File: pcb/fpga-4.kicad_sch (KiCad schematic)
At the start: 1 part, among them U5 XC7A100T-FGG484

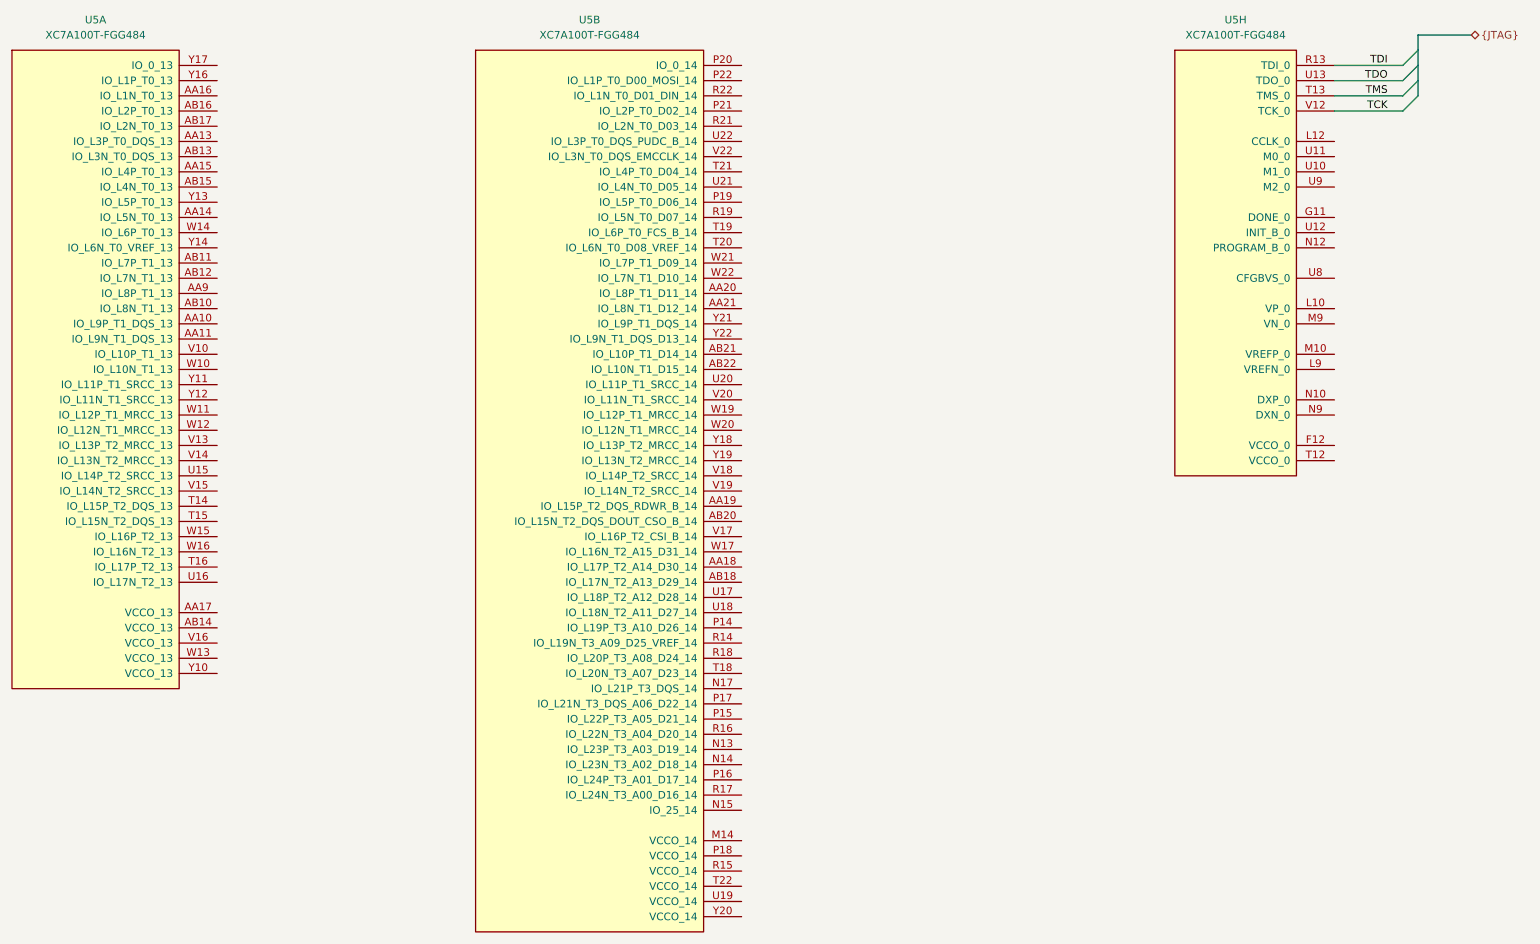
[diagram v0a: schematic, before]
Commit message: defined memory pinouts
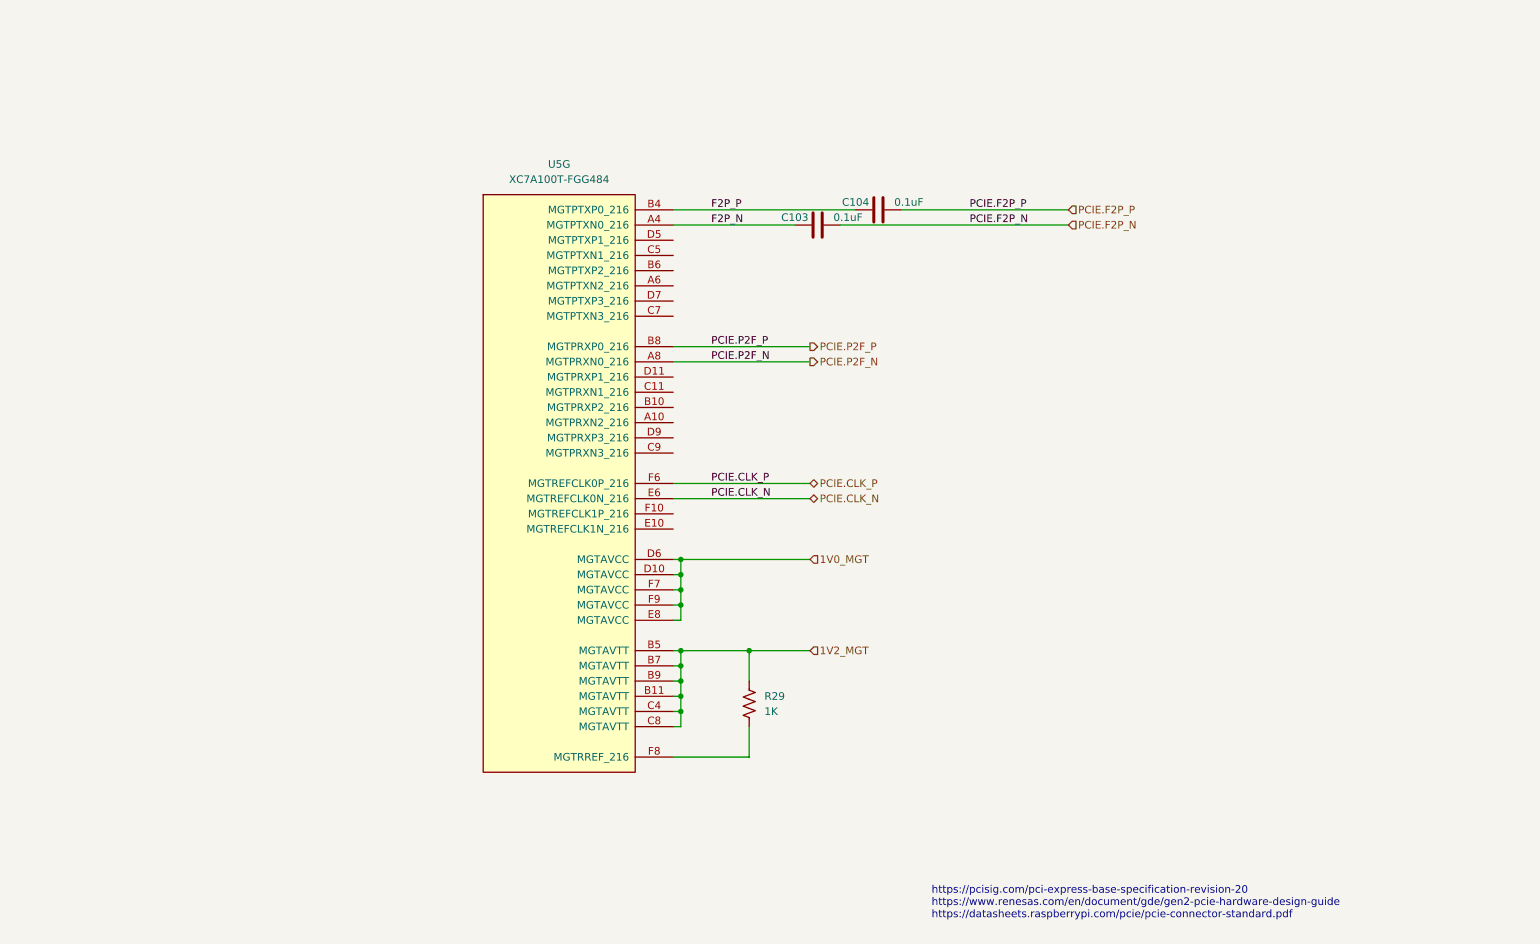
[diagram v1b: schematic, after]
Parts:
- removed U5: XC7A100T-FGG484, library:Xilinx_FGG484, symbol FPGA_Xilinx_Artix7:XC7A100T-FGG484
- added C103, C104: 0.1uF, Capacitor_SMD:C_0402_1005Metric, symbol library:C
- added R29: 1K, symbol library:R_US
- added U5: XC7A100T-FGG484, library:Xilinx_FGG484, symbol FPGA_Xilinx_Artix7:XC7A100T-FGG484
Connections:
- new net: R29.1, U5.F8 (MGTRREF_216)
- new net 1V0_MGT: U5.D10 (MGTAVCC), U5.D6 (MGTAVCC), U5.E8 (MGTAVCC), U5.F7 (MGTAVCC), U5.F9 (MGTAVCC)
- new net 1V2_MGT: R29.2, U5.B11 (MGTAVTT), U5.B5 (MGTAVTT), U5.B7 (MGTAVTT), U5.B9 (MGTAVTT), U5.C4 (MGTAVTT), U5.C8 (MGTAVTT)
- new net F2P_N: C103.1, U5.A4 (MGTPTXN0_216)
- new net F2P_P: C104.1, U5.B4 (MGTPTXP0_216)
- new net PCIE.CLK_N: U5.E6 (MGTREFCLK0N_216)
- new net PCIE.CLK_P: U5.F6 (MGTREFCLK0P_216)
- new net PCIE.F2P_N: C103.2
- new net PCIE.F2P_P: C104.2
- new net PCIE.P2F_N: U5.A8 (MGTPRXN0_216)
- new net PCIE.P2F_P: U5.B8 (MGTPRXP0_216)
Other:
- note added: "https://pcisig.com/pci-express-base-specification-revision-20 https://www.renesas.com/en/document/gde/gen2-pcie-hardware-design-guide https://datasheets.raspberrypi.com/pcie/pcie-connector-standard.pdf"

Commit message: power restructuring
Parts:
- removed C103, C104: 0.1uF, Capacitor_SMD:C_0402_1005Metric, symbol library:C
- added C11, C12: 0.1uF, Capacitor_SMD:C_0402_1005Metric, symbol library:C
- U5: symbol FPGA_Xilinx_Artix7:XC7A100T-FGG484 -> library:XC7A100T-FGG484
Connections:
- net F2P_N: now also C11.1
- net F2P_P: now also C12.1
- net PCIE.F2P_N: now also C11.2
- net PCIE.F2P_P: now also C12.2
- net at U5.F8 (MGTRREF_216): no longer R29.1
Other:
- moved on the sheet: R29, U5G

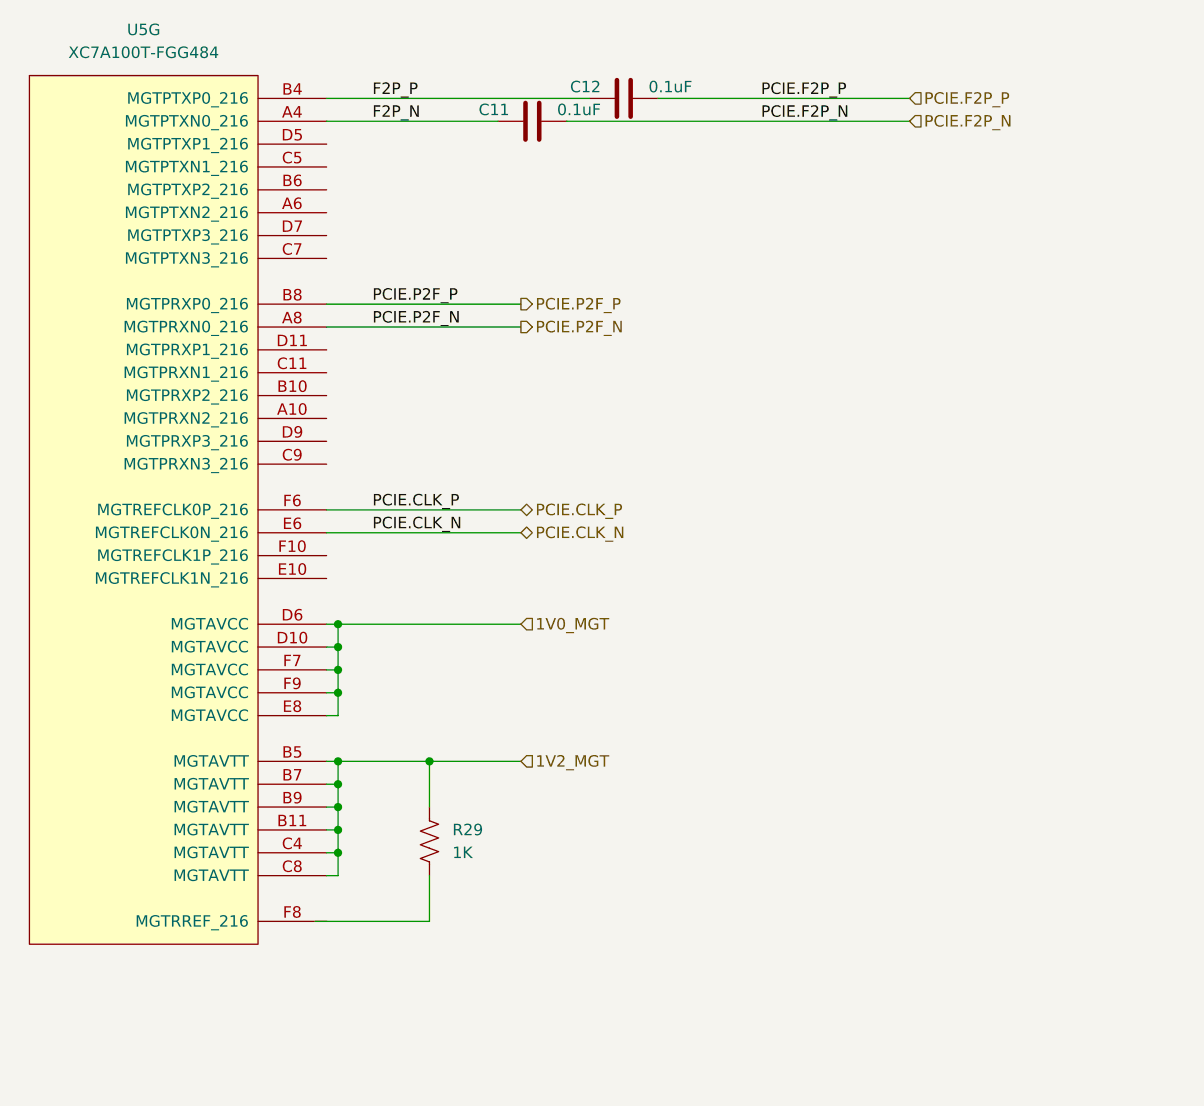
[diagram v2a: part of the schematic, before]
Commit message: changes to power tree
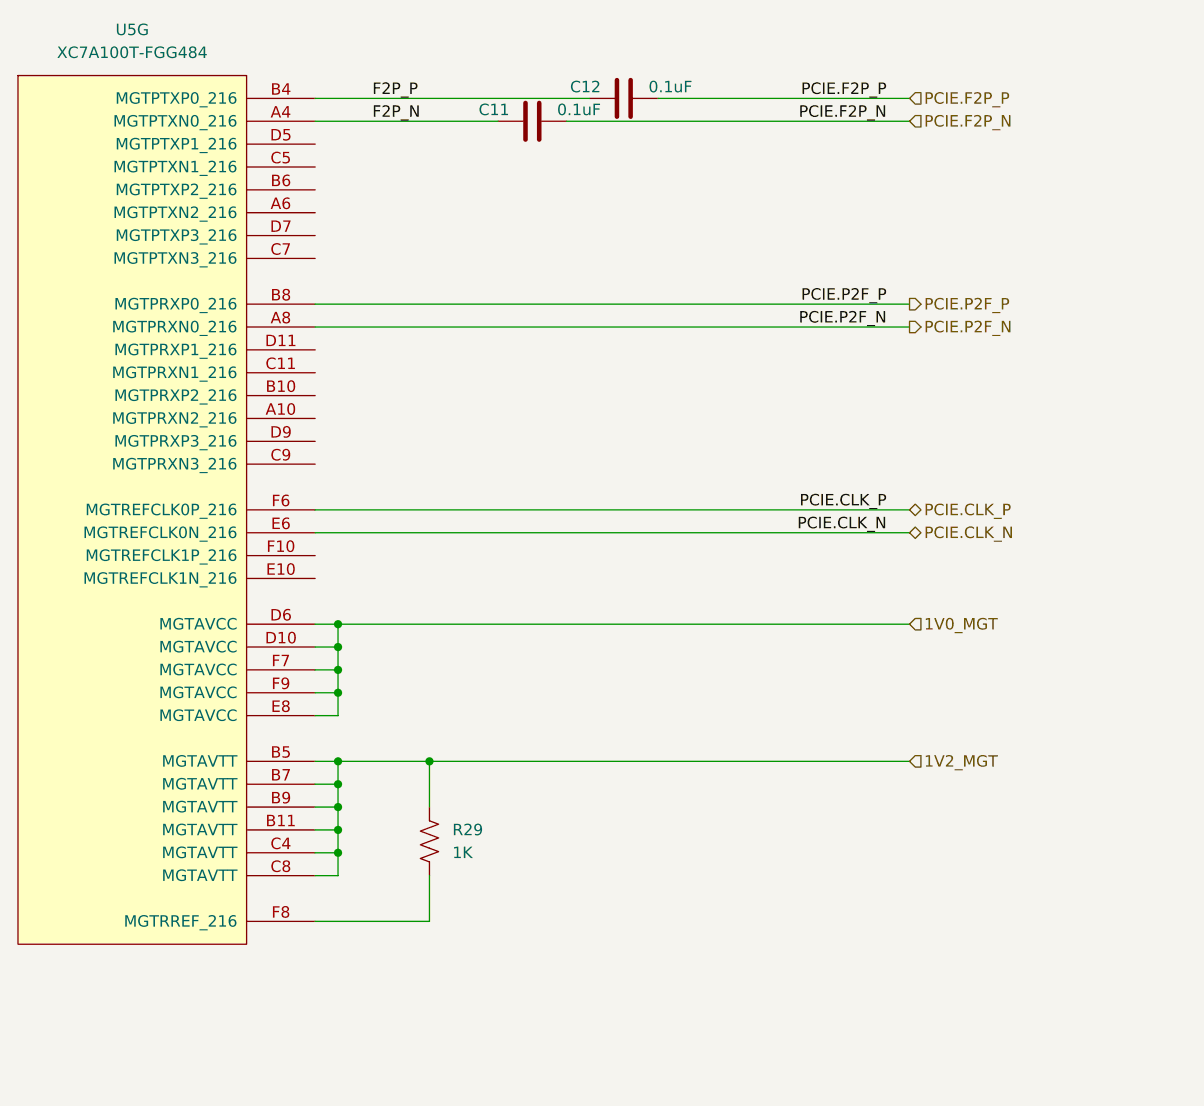
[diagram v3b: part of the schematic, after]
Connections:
- net at U5.F8 (MGTRREF_216): now also R29.1
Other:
- moved on the sheet: U5G

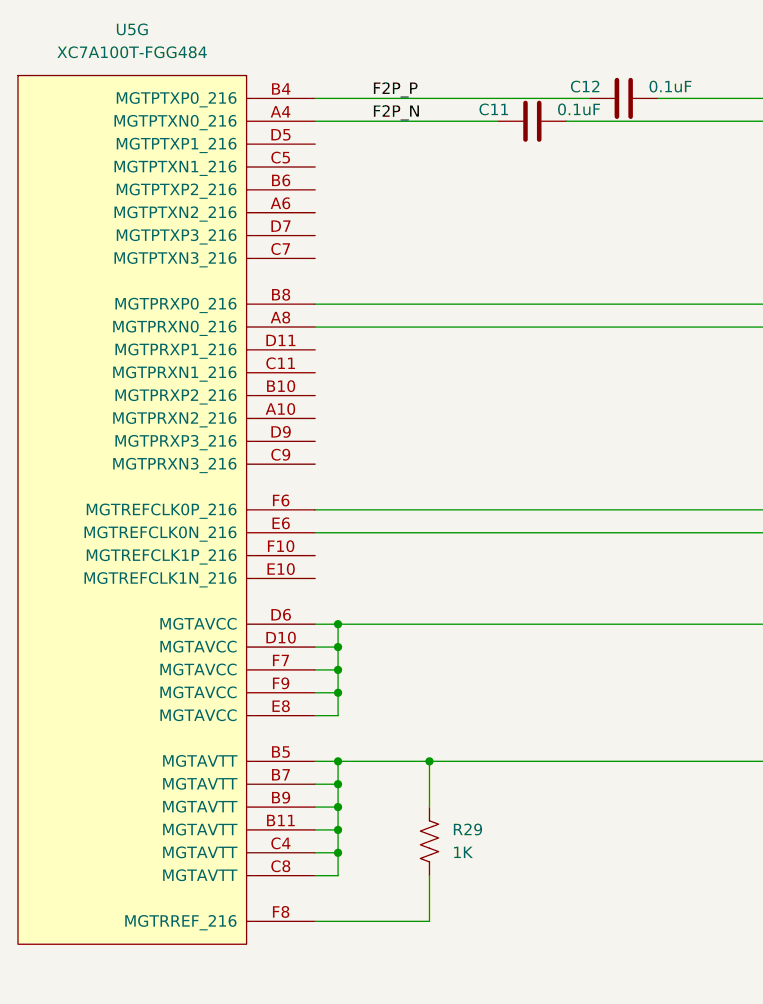
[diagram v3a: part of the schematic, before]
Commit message: moved stuff around, bom
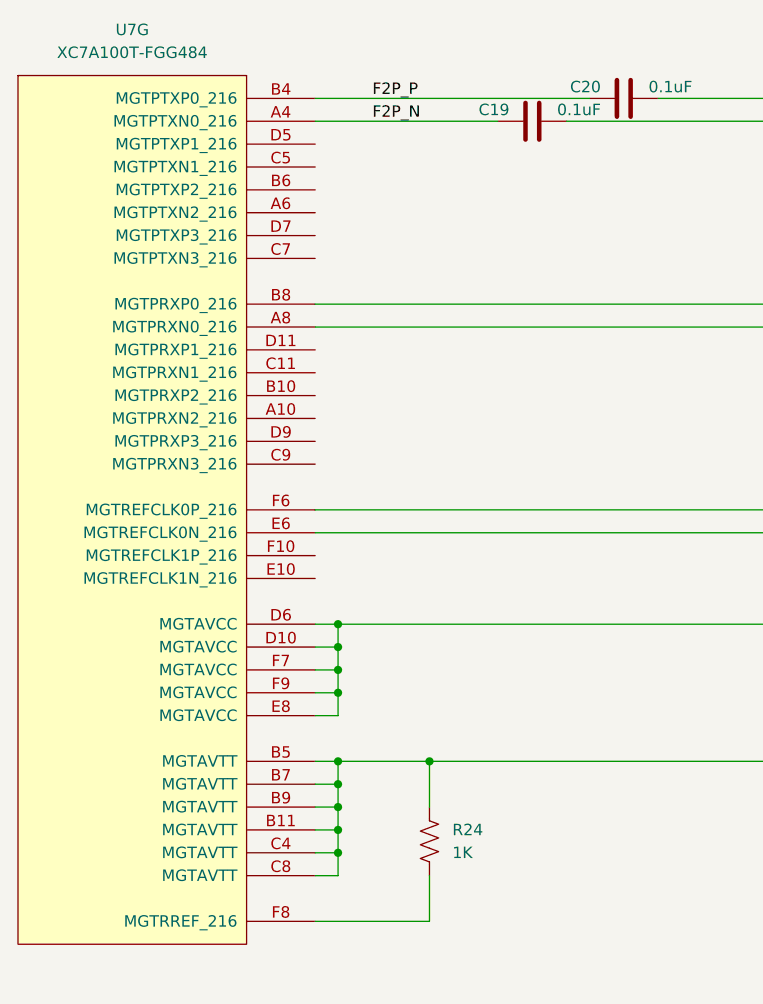
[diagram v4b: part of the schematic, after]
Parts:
- renumbered C11 to C19, C12 to C20, R29 to R24, U5 to U7
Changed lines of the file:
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@@
 		(dnp no)
 		(fields_autoplaced yes)
-		(property "Reference" "U5"
+		(property "Reference" "U7"
 			(at 114.3 45.72 0)
 			(effects
@@
 			(project "RPi-HwAB-1"
 				(path "/e63e39d7-6ac0-4ffd-8aa3-1841a4541b55/59d21473-a004-4514-8090-fd93db818925/1a53bf83-d036-4e40-a4d5-3697b8dd72a6"
-					(reference "U5")
+					(reference "U7")
 					(unit 7)
 				)
@@
 		(dnp no)
 		(fields_autoplaced yes)
-		(property "Reference" "R29"
+		(property "Reference" "R24"
 			(at 149.86 134.6199 0)
 			(effects
@@
 			(project "RPi-HwAB-1"
 				(path "/e63e39d7-6ac0-4ffd-8aa3-1841a4541b55/59d21473-a004-4514-8090-fd93db818925/1a53bf83-d036-4e40-a4d5-3697b8dd72a6"
-					(reference "R29")
+					(reference "R24")
 					(unit 1)
 				)
@@
 		(on_board yes)
 		(dnp no)
-		(property "Reference" "C12"
+		(property "Reference" "C20"
 			(at 166.37 52.07 90)
 			(effects
@@
 			(project "RPi-HwAB-1"
 				(path "/e63e39d7-6ac0-4ffd-8aa3-1841a4541b55/59d21473-a004-4514-8090-fd93db818925/1a53bf83-d036-4e40-a4d5-3697b8dd72a6"
-					(reference "C12")
+					(reference "C20")
 					(unit 1)
 				)
@@
 		(on_board yes)
 		(dnp no)
-		(property "Reference" "C11"
+		(property "Reference" "C19"
 			(at 156.21 54.61 90)
 			(effects
@@
 			(project "RPi-HwAB-1"
 				(path "/e63e39d7-6ac0-4ffd-8aa3-1841a4541b55/59d21473-a004-4514-8090-fd93db818925/1a53bf83-d036-4e40-a4d5-3697b8dd72a6"
-					(reference "C11")
+					(reference "C19")
 					(unit 1)
 				)

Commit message: decoupling
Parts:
- added C110, C111, C112, C113, C114, C152, C153, C154, C155, C156, C157: 0.1uF, Capacitor_SMD:C_0402_1005Metric, symbol library:C
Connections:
- net 1V0_MGT: now also C110.2, C111.2, C112.2, C113.2, C114.2
- net 1V2_MGT: now also C152.2, C153.2, C154.2, C155.2, C156.2, C157.2
- new net GND: C110.1, C111.1, C112.1, C113.1, C114.1, C152.1, C153.1, C154.1, C155.1, C156.1, C157.1

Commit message: bom
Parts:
- C56: renamed from C114; Part Description (none) -> CAP CER 0.1UF 16V X7R 0402
- C57: renamed from C157; Part Description (none) -> CAP CER 0.1UF 16V X7R 0402
- C58: renamed from C113; Part Description (none) -> CAP CER 0.1UF 16V X7R 0402
- C59: renamed from C156; Part Description (none) -> CAP CER 0.1UF 16V X7R 0402
- C60: renamed from C112; Part Description (none) -> CAP CER 0.1UF 16V X7R 0402
- C61: renamed from C155; Part Description (none) -> CAP CER 0.1UF 16V X7R 0402
- C62: renamed from C111; Part Description (none) -> CAP CER 0.1UF 16V X7R 0402
- C63: renamed from C154; Part Description (none) -> CAP CER 0.1UF 16V X7R 0402
- C64: renamed from C110; Part Description (none) -> CAP CER 0.1UF 16V X7R 0402
- C65: renamed from C153; Part Description (none) -> CAP CER 0.1UF 16V X7R 0402
- C66: renamed from C152; Part Description (none) -> CAP CER 0.1UF 16V X7R 0402
- C67: renamed from C19; Part Description 0.1uF 10% 16V Ceramic Capacitor X7R 0402 (1005 Metric) -> CAP CER 0.1UF 16V X7R 0402
- C68: renamed from C20; Part Description 0.1uF 10% 16V Ceramic Capacitor X7R 0402 (1005 Metric) -> CAP CER 0.1UF 16V X7R 0402
- R25: renamed from R24; footprint (none) -> Resistor_SMD:R_0402_1005Metric; Manufacturer (none) -> Vishay Dale; Manufacturer Product Number (none) -> CRCW04021K00FKED; Part Description (none) -> RES 1K OHM 1% 1/16W 0402
- U7: Manufacturer (none) -> AMD; Manufacturer Product Number (none) -> XC7A100T-1FGG484C; Part Description (none) -> IC FPGA 285 I/O 484FBGA
